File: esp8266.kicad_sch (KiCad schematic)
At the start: 17 parts, among them J7 Conn_01x06_Pin, U11 ISO7321C, U6 ESP-12F, U7 PC817, U8 PC817

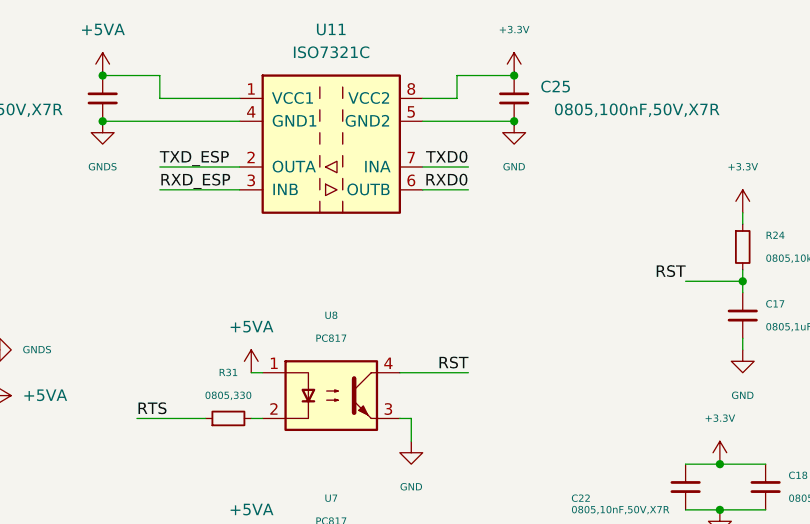
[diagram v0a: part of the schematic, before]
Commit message: [A02] Edited R4, R5
R4 20k -> 10k since nothing else uses 20k
R5 10k -> 510k to reduce D3 LED brightness
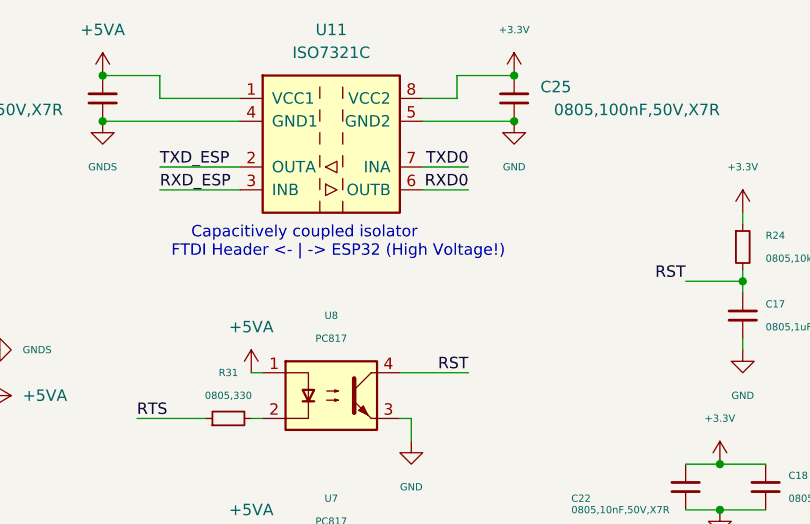
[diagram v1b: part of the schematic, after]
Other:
- note added: "Capacitively coupled isolator FTDI Header <- | -> ESP32 (High Voltage!)"
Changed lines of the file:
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@@
   (paper "USLetter")
   (title_block
-    (date "2023-12-18")
-    (rev "A01")
+    (date "2023-12-30")
+    (rev "A02")
   )
   (junction (at 157.48 171.45) (diameter 0) (color 0 0 0 0)
@@
     (stroke (width 0) (type default))
   )
+  (text "    Capacitively coupled isolator\nFTDI Header <- | -> ESP32 (High Voltage!)"
+    (at 60.96 137.16 0)
+    (effects (font (size 1.27 1.27)) (justify left bottom))
+  )
   (label "GPIO0" (at 172.72 137.16 0) (fields_autoplaced)
